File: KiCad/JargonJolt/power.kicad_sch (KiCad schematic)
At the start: 0 parts

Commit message: worked on schematic
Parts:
- added C5, C6: C, Capacitor_SMD:C_0805_2012Metric, symbol Device:C
- added J2, J3: Conn_01x02, symbol Connector_Generic:Conn_01x02
- added JP2: SolderJumper_3_Open, symbol Jumper:SolderJumper_3_Open
- added SW4: SW_DIP_x01, symbol Switch:SW_DIP_x01
- added U4: ADP3339, Package_TO_SOT_SMD:SOT-223-3_TabPin2, symbol Regulator_Linear:AMS1117-3.3
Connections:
- new net: JP2.2 (C), U4.3 (VI)
- new net +12V: J3.1 (Pin_1), JP2.3 (B)
- new net +3.3V: C5.1, SW4.1, U4.2 (VO)
- new net +3.3VA: C6.1, SW4.2
- new net +3.7V: J2.1 (Pin_1)
- new net +3V7: JP2.1 (A)
- new net GND: C5.2, C6.2, J2.2 (Pin_2), J3.2 (Pin_2), U4.1 (GND)
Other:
- note added: "Barrel Jack Conn"
- note added: "Battery Conn"

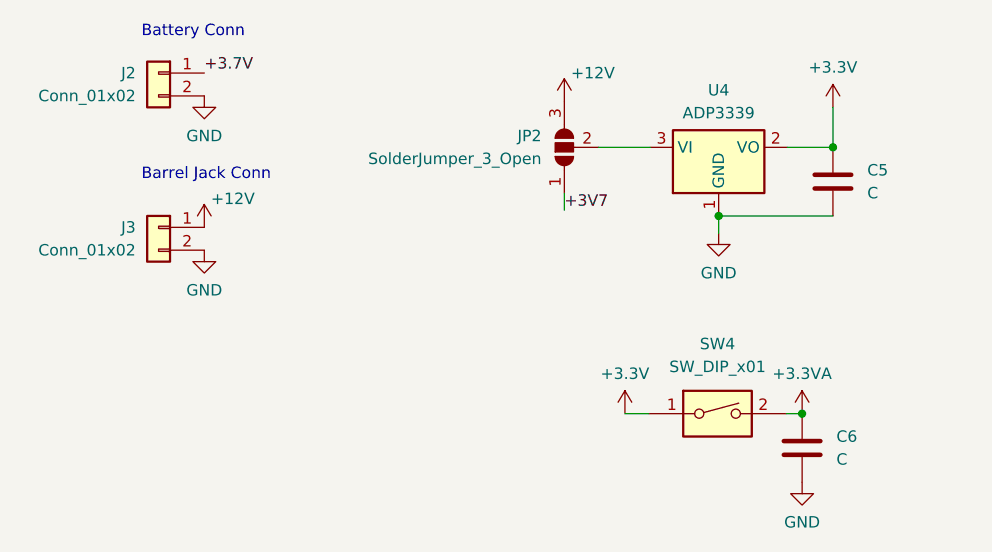
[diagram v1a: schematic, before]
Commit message: added sd module + fixed CS pins
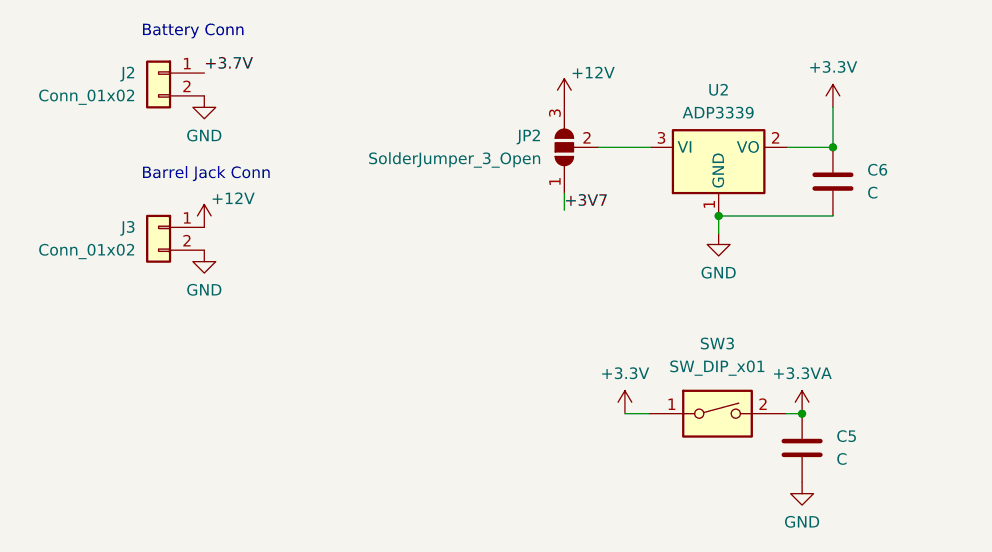
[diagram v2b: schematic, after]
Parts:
- renumbered C6 to C5, C5 to C6, SW4 to SW3, U4 to U2
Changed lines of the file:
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@@
   (symbol (lib_id "power:GND") (at 112.395 90.805 0) (unit 1)
     (in_bom yes) (on_board yes) (dnp no) (fields_autoplaced)
-    (property "Reference" "#PWR026" (at 112.395 97.155 0)
+    (property "Reference" "#PWR018" (at 112.395 97.155 0)
       (effects (font (size 1.27 1.27)) hide)
     )
@@
       (project "JargonJolt"
         (path "/39fa52d1-bab8-41e3-aba2-e2f783adaf1f/a91347d5-40c0-4d74-a0b7-7f14df56e886"
-          (reference "#PWR026") (unit 1)
+          (reference "#PWR018") (unit 1)
         )
       )
@@
   (symbol (lib_id "power:+3.3VA") (at 121.666 110.871 0) (unit 1)
     (in_bom yes) (on_board yes) (dnp no) (fields_autoplaced)
-    (property "Reference" "#PWR032" (at 121.666 114.681 0)
+    (property "Reference" "#PWR019" (at 121.666 114.681 0)
       (effects (font (size 1.27 1.27)) hide)
     )
@@
       (project "JargonJolt"
         (path "/39fa52d1-bab8-41e3-aba2-e2f783adaf1f/a91347d5-40c0-4d74-a0b7-7f14df56e886"
-          (reference "#PWR032") (unit 1)
+          (reference "#PWR019") (unit 1)
         )
       )
@@
   (symbol (lib_id "power:+3.3V") (at 125.095 76.835 0) (unit 1)
     (in_bom yes) (on_board yes) (dnp no) (fields_autoplaced)
-    (property "Reference" "#PWR027" (at 125.095 80.645 0)
+    (property "Reference" "#PWR021" (at 125.095 80.645 0)
       (effects (font (size 1.27 1.27)) hide)
     )
@@
       (project "JargonJolt"
         (path "/39fa52d1-bab8-41e3-aba2-e2f783adaf1f/a91347d5-40c0-4d74-a0b7-7f14df56e886"
-          (reference "#PWR027") (unit 1)
+          (reference "#PWR021") (unit 1)
         )
       )
@@
   (symbol (lib_id "Device:C") (at 125.095 85.09 0) (unit 1)
     (in_bom yes) (on_board yes) (dnp no) (fields_autoplaced)
-    (property "Reference" "C5" (at 128.905 83.82 0)
+    (property "Reference" "C6" (at 128.905 83.82 0)
       (effects (font (size 1.27 1.27)) (justify left))
     )
@@
       (project "JargonJolt"
         (path "/39fa52d1-bab8-41e3-aba2-e2f783adaf1f/a91347d5-40c0-4d74-a0b7-7f14df56e886"
-          (reference "C5") (unit 1)
+          (reference "C6") (unit 1)
         )
       )
@@
   (symbol (lib_id "power:+12V") (at 55.245 90.17 0) (unit 1)
     (in_bom yes) (on_board yes) (dnp no)
-    (property "Reference" "#PWR023" (at 55.245 93.98 0)
+    (property "Reference" "#PWR014" (at 55.245 93.98 0)
       (effects (font (size 1.27 1.27)) hide)
     )
@@
       (project "JargonJolt"
         (path "/39fa52d1-bab8-41e3-aba2-e2f783adaf1f/a91347d5-40c0-4d74-a0b7-7f14df56e886"
-          (reference "#PWR023") (unit 1)
+          (reference "#PWR014") (unit 1)
         )
       )
@@
   (symbol (lib_id "power:GND") (at 55.245 75.565 0) (unit 1)
     (in_bom yes) (on_board yes) (dnp no) (fields_autoplaced)
-    (property "Reference" "#PWR022" (at 55.245 81.915 0)
+    (property "Reference" "#PWR013" (at 55.245 81.915 0)
       (effects (font (size 1.27 1.27)) hide)
     )
@@
       (project "JargonJolt"
         (path "/39fa52d1-bab8-41e3-aba2-e2f783adaf1f/a91347d5-40c0-4d74-a0b7-7f14df56e886"
-          (reference "#PWR022") (unit 1)
+          (reference "#PWR013") (unit 1)
         )
       )
@@
   (symbol (lib_id "power:GND") (at 121.666 118.491 0) (unit 1)
     (in_bom yes) (on_board yes) (dnp no) (fields_autoplaced)
-    (property "Reference" "#PWR034" (at 121.666 124.841 0)
+    (property "Reference" "#PWR020" (at 121.666 124.841 0)
       (effects (font (size 1.27 1.27)) hide)
     )
@@
       (project "JargonJolt"
         (path "/39fa52d1-bab8-41e3-aba2-e2f783adaf1f/a91347d5-40c0-4d74-a0b7-7f14df56e886"
-          (reference "#PWR034") (unit 1)
+          (reference "#PWR020") (unit 1)
         )
       )
@@
   (symbol (lib_id "power:+12V") (at 95.25 76.2 0) (unit 1)
     (in_bom yes) (on_board yes) (dnp no)
-    (property "Reference" "#PWR025" (at 95.25 80.01 0)
+    (property "Reference" "#PWR016" (at 95.25 80.01 0)
       (effects (font (size 1.27 1.27)) hide)
     )
@@
       (project "JargonJolt"
         (path "/39fa52d1-bab8-41e3-aba2-e2f783adaf1f/a91347d5-40c0-4d74-a0b7-7f14df56e886"
-          (reference "#PWR025") (unit 1)
+          (reference "#PWR016") (unit 1)
         )
       )
@@
   (symbol (lib_id "Device:C") (at 121.666 114.681 0) (unit 1)
     (in_bom yes) (on_board yes) (dnp no) (fields_autoplaced)
-    (property "Reference" "C6" (at 125.476 113.411 0)
+    (property "Reference" "C5" (at 125.476 113.411 0)
       (effects (font (size 1.27 1.27)) (justify left))
     )
@@
       (project "JargonJolt"
         (path "/39fa52d1-bab8-41e3-aba2-e2f783adaf1f/a91347d5-40c0-4d74-a0b7-7f14df56e886"
-          (reference "C6") (unit 1)
+          (reference "C5") (unit 1)
         )
       )
@@
   (symbol (lib_id "Switch:SW_DIP_x01") (at 112.268 110.871 0) (unit 1)
     (in_bom yes) (on_board yes) (dnp no) (fields_autoplaced)
-    (property "Reference" "SW4" (at 112.268 103.124 0)
+    (property "Reference" "SW3" (at 112.268 103.124 0)
       (effects (font (size 1.27 1.27)))
     )
@@
       (project "JargonJolt"
         (path "/39fa52d1-bab8-41e3-aba2-e2f783adaf1f/a91347d5-40c0-4d74-a0b7-7f14df56e886"
-          (reference "SW4") (unit 1)
+          (reference "SW3") (unit 1)
         )
       )
@@
   (symbol (lib_id "power:GND") (at 55.245 92.71 0) (unit 1)
     (in_bom yes) (on_board yes) (dnp no) (fields_autoplaced)
-    (property "Reference" "#PWR024" (at 55.245 99.06 0)
+    (property "Reference" "#PWR015" (at 55.245 99.06 0)
       (effects (font (size 1.27 1.27)) hide)
     )
@@
       (project "JargonJolt"
         (path "/39fa52d1-bab8-41e3-aba2-e2f783adaf1f/a91347d5-40c0-4d74-a0b7-7f14df56e886"
-          (reference "#PWR024") (unit 1)
+          (reference "#PWR015") (unit 1)
         )
       )
@@
   (symbol (lib_id "power:+3.3V") (at 101.981 110.871 0) (unit 1)
     (in_bom yes) (on_board yes) (dnp no) (fields_autoplaced)
-    (property "Reference" "#PWR021" (at 101.981 114.681 0)
+    (property "Reference" "#PWR017" (at 101.981 114.681 0)
       (effects (font (size 1.27 1.27)) hide)
     )
@@
       (project "JargonJolt"
         (path "/39fa52d1-bab8-41e3-aba2-e2f783adaf1f/a91347d5-40c0-4d74-a0b7-7f14df56e886"
-          (reference "#PWR021") (unit 1)
+          (reference "#PWR017") (unit 1)
         )
       )
@@
   (symbol (lib_id "Regulator_Linear:AMS1117-3.3") (at 112.395 81.28 0) (unit 1)
     (in_bom yes) (on_board yes) (dnp no) (fields_autoplaced)
-    (property "Reference" "U4" (at 112.395 74.93 0)
+    (property "Reference" "U2" (at 112.395 74.93 0)
       (effects (font (size 1.27 1.27)))
     )
@@
       (project "JargonJolt"
         (path "/39fa52d1-bab8-41e3-aba2-e2f783adaf1f/a91347d5-40c0-4d74-a0b7-7f14df56e886"
-          (reference "U4") (unit 1)
-        )
-      )
+          (reference "U2") (unit 1)
+        )
+      )

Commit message: PCB first revision
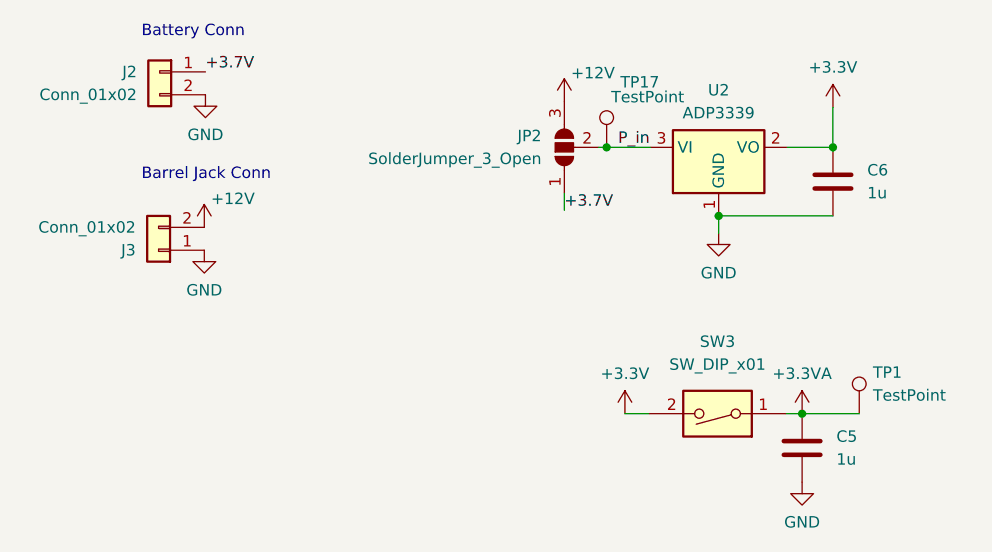
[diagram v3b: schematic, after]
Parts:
- added TP1, TP17: TestPoint, TestPoint:TestPoint_Pad_D1.5mm, symbol Connector:TestPoint
- C5, C6: value C -> 1u
- J2, SW3: footprint (none) -> Connector_Molex:Molex_KK-254_AE-6410-02A_1x02_P2.54mm_Vertical
- J3: footprint (none) -> Connector_BarrelJack:BarrelJack_Horizontal
- JP2: footprint (none) -> Jumper:SolderJumper-3_P1.3mm_Open_RoundedPad1.0x1.5mm
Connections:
- net +3V7 is gone; now on net +3.7V: JP2.1 (A)
- net +12V: now also J3.2 (Pin_2); no longer J3.1 (Pin_1)
- net +3.3V: now also SW3.2; no longer SW3.1
- net +3.3VA: now also SW3.1, TP1.1; no longer SW3.2
- net GND: now also J3.1 (Pin_1); no longer J3.2 (Pin_2)
- net P_in: now reaches JP2.2 (C), U2.3 (VI)
- net P_in: now also TP17.1
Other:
- moved on the sheet: J3, SW3
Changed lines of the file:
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@@
   (junction (at 112.395 88.9) (diameter 0) (color 0 0 0 0)
   )
+  (junction (at 99.949 81.28) (diameter 0) (color 0 0 0 0)
+  )
   (junction (at 125.095 81.28) (diameter 0) (color 0 0 0 0)
   )
@@
     (stroke (width 0) (type default))
   )
+  (wire (pts (xy 99.949 81.28) (xy 99.06 81.28))
+    (stroke (width 0) (type default))
+  )
   (wire (pts (xy 101.981 110.871) (xy 104.648 110.871))
     (stroke (width 0) (type default))
@@
     (stroke (width 0) (type default))
   )
-  (wire (pts (xy 104.775 81.28) (xy 99.06 81.28))
+  (wire (pts (xy 121.666 110.871) (xy 128.016 110.871))
+    (stroke (width 0) (type default))
+  )
+  (wire (pts (xy 104.775 81.28) (xy 99.949 81.28))
     (stroke (width 0) (type default))
   )
@@
     (effects (font (size 1.27 1.27)) (justify left bottom))
   )
-  (label "+3V7" (at 95.25 88.265 0) (fields_autoplaced)
+  (label "P_in" (at 101.219 81.28 0) (fields_autoplaced)
     (effects (font (size 1.27 1.27)) (justify left bottom))
   )
-  (label "+3.7V" (at 55.245 73.025 0) (fields_autoplaced)
+  (label "+3.7V" (at 95.25 88.265 0) (fields_autoplaced)
     (effects (font (size 1.27 1.27)) (justify left bottom))
   )
+  (label "+3.7V" (at 55.372 72.898 0) (fields_autoplaced)
+    (effects (font (size 1.27 1.27)) (justify left bottom))
+  )
   (symbol (lib_id "power:GND") (at 112.395 90.805 0) (unit 1)
     (in_bom yes) (on_board yes) (dnp no) (fields_autoplaced)
@@
       (effects (font (size 1.27 1.27)) (justify left))
     )
-    (property "Value" "C" (at 128.905 86.36 0)
+    (property "Value" "1u" (at 128.905 86.36 0)
       (effects (font (size 1.27 1.27)) (justify left))
     )
@@
     )
   )
-  (symbol (lib_id "power:GND") (at 55.245 75.565 0) (unit 1)
-    (in_bom yes) (on_board yes) (dnp no) (fields_autoplaced)
-    (property "Reference" "#PWR013" (at 55.245 81.915 0)
-      (effects (font (size 1.27 1.27)) hide)
-    )
-    (property "Value" "GND" (at 55.245 80.01 0)
-      (effects (font (size 1.27 1.27)))
-    )
-    (property "Footprint" "" (at 55.245 75.565 0)
-      (effects (font (size 1.27 1.27)) hide)
-    )
-    (property "Datasheet" "" (at 55.245 75.565 0)
+  (symbol (lib_id "power:GND") (at 55.372 75.438 0) (unit 1)
+    (in_bom yes) (on_board yes) (dnp no) (fields_autoplaced)
+    (property "Reference" "#PWR013" (at 55.372 81.788 0)
+      (effects (font (size 1.27 1.27)) hide)
+    )
+    (property "Value" "GND" (at 55.372 79.883 0)
+      (effects (font (size 1.27 1.27)))
+    )
+    (property "Footprint" "" (at 55.372 75.438 0)
+      (effects (font (size 1.27 1.27)) hide)
+    )
+    (property "Datasheet" "" (at 55.372 75.438 0)
       (effects (font (size 1.27 1.27)) hide)
     )
@@
       (effects (font (size 1.27 1.27)) (justify left))
     )
-    (property "Footprint" "" (at 95.25 81.28 0)
+    (property "Footprint" "Jumper:SolderJumper-3_P1.3mm_Open_RoundedPad1.0x1.5mm" (at 95.25 81.28 0)
       (effects (font (size 1.27 1.27)) hide)
     )
@@
       (effects (font (size 1.27 1.27)) (justify left))
     )
-    (property "Value" "C" (at 125.476 115.951 0)
+    (property "Value" "1u" (at 125.476 115.951 0)
       (effects (font (size 1.27 1.27)) (justify left))
     )
@@
     )
   )
-  (symbol (lib_id "Switch:SW_DIP_x01") (at 112.268 110.871 0) (unit 1)
-    (in_bom yes) (on_board yes) (dnp no) (fields_autoplaced)
-    (property "Reference" "SW3" (at 112.268 103.124 0)
-      (effects (font (size 1.27 1.27)))
-    )
-    (property "Value" "SW_DIP_x01" (at 112.268 105.664 0)
-      (effects (font (size 1.27 1.27)))
-    )
-    (property "Footprint" "" (at 112.268 110.871 0)
+  (symbol (lib_id "Connector:TestPoint") (at 99.949 81.28 0) (unit 1)
+    (in_bom yes) (on_board yes) (dnp no)
+    (property "Reference" "TP17" (at 101.473 74.041 0)
+      (effects (font (size 1.27 1.27)) (justify left))
+    )
+    (property "Value" "TestPoint" (at 100.457 75.692 0)
+      (effects (font (size 1.27 1.27)) (justify left))
+    )
+    (property "Footprint" "TestPoint:TestPoint_Pad_D1.5mm" (at 105.029 81.28 0)
+      (effects (font (size 1.27 1.27)) hide)
+    )
+    (property "Datasheet" "~" (at 105.029 81.28 0)
+      (effects (font (size 1.27 1.27)) hide)
+    )
+    (pin "1")
+    (instances
+      (project "JargonJolt"
+        (path "/39fa52d1-bab8-41e3-aba2-e2f783adaf1f/a91347d5-40c0-4d74-a0b7-7f14df56e886"
+          (reference "TP17") (unit 1)
+        )
+      )
+    )
+  )
+  (symbol (lib_id "Switch:SW_DIP_x01") (at 112.268 110.871 180) (unit 1)
+    (in_bom yes) (on_board yes) (dnp no) (fields_autoplaced)
+    (property "Reference" "SW3" (at 112.268 102.87 0)
+      (effects (font (size 1.27 1.27)))
+    )
+    (property "Value" "SW_DIP_x01" (at 112.268 105.41 0)
+      (effects (font (size 1.27 1.27)))
+    )
+    (property "Footprint" "Connector_Molex:Molex_KK-254_AE-6410-02A_1x02_P2.54mm_Vertical" (at 112.268 110.871 0)
       (effects (font (size 1.27 1.27)) hide)
     )
@@
     )
   )
+  (symbol (lib_id "Connector:TestPoint") (at 128.016 110.871 0) (unit 1)
+    (in_bom yes) (on_board yes) (dnp no) (fields_autoplaced)
+    (property "Reference" "TP1" (at 129.54 106.299 0)
+      (effects (font (size 1.27 1.27)) (justify left))
+    )
+    (property "Value" "TestPoint" (at 129.54 108.839 0)
+      (effects (font (size 1.27 1.27)) (justify left))
+    )
+    (property "Footprint" "TestPoint:TestPoint_Pad_D1.5mm" (at 133.096 110.871 0)
+      (effects (font (size 1.27 1.27)) hide)
+    )
+    (property "Datasheet" "~" (at 133.096 110.871 0)
+      (effects (font (size 1.27 1.27)) hide)
+    )
+    (pin "1")
+    (instances
+      (project "JargonJolt"
+        (path "/39fa52d1-bab8-41e3-aba2-e2f783adaf1f/a91347d5-40c0-4d74-a0b7-7f14df56e886"
+          (reference "TP1") (unit 1)
+        )
+      )
+    )
+  )
   (symbol (lib_id "power:GND") (at 55.245 92.71 0) (unit 1)
     (in_bom yes) (on_board yes) (dnp no) (fields_autoplaced)
@@
     )
   )
-  (symbol (lib_id "Connector_Generic:Conn_01x02") (at 50.165 73.025 0) (mirror y) (unit 1)
+  (symbol (lib_id "Connector_Generic:Conn_01x02") (at 50.292 72.898 0) (mirror y) (unit 1)
     (in_bom yes) (on_board yes) (dnp no)
-    (property "Reference" "J2" (at 47.625 73.025 0)
-      (effects (font (size 1.27 1.27)) (justify left))
-    )
-    (property "Value" "Conn_01x02" (at 47.625 75.565 0)
-      (effects (font (size 1.27 1.27)) (justify left))
-    )
-    (property "Footprint" "" (at 50.165 73.025 0)
-      (effects (font (size 1.27 1.27)) hide)
-    )
-    (property "Datasheet" "~" (at 50.165 73.025 0)
+    (property "Reference" "J2" (at 47.752 72.898 0)
+      (effects (font (size 1.27 1.27)) (justify left))
+    )
+    (property "Value" "Conn_01x02" (at 47.752 75.438 0)
+      (effects (font (size 1.27 1.27)) (justify left))
+    )
+    (property "Footprint" "Connector_Molex:Molex_KK-254_AE-6410-02A_1x02_P2.54mm_Vertical" (at 50.292 72.898 0)
+      (effects (font (size 1.27 1.27)) hide)
+    )
+    (property "Datasheet" "~" (at 50.292 72.898 0)
       (effects (font (size 1.27 1.27)) hide)
     )
@@
     )
   )
-  (symbol (lib_id "Connector_Generic:Conn_01x02") (at 50.165 90.17 0) (mirror y) (unit 1)
+  (symbol (lib_id "Connector_Generic:Conn_01x02") (at 50.165 92.71 180) (unit 1)
     (in_bom yes) (on_board yes) (dnp no)
-    (property "Reference" "J3" (at 47.625 90.17 0)
-      (effects (font (size 1.27 1.27)) (justify left))
-    )
-    (property "Value" "Conn_01x02" (at 47.625 92.71 0)
-      (effects (font (size 1.27 1.27)) (justify left))
-    )
-    (property "Footprint" "" (at 50.165 90.17 0)
-      (effects (font (size 1.27 1.27)) hide)
-    )
-    (property "Datasheet" "~" (at 50.165 90.17 0)
-      (effects (font (size 1.27 1.27)) hide)
-    )
+    (property "Reference" "J3" (at 47.625 92.71 0)
+      (effects (font (size 1.27 1.27)) (justify left))
+    )
+    (property "Value" "Conn_01x02" (at 47.625 90.17 0)
+      (effects (font (size 1.27 1.27)) (justify left))
+    )
+    (property "Footprint" "Connector_BarrelJack:BarrelJack_Horizontal" (at 50.165 92.71 0)
+      (effects (font (size 1.27 1.27)) hide)
+    )
+    (property "Datasheet" "https://www.cuidevices.com/product/resource/pj-102ah.pdf" (at 50.165 92.71 0)
+      (effects (font (size 1.27 1.27)) hide)
+    )
